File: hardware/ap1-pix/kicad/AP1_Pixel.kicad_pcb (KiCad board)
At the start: 2 copper layers, 88 x 56 mm, 43 parts, among them J1 ENTRADA 5-24V, J2 PIXELES 1, J3 PIXELES 2, J4 PIXELES 3, J5 PIXELES 4, J7 PROGRAMADOR, U1 INA238, U2 LMR16006XDDC, U3 74HCT125D, U4 M24C02-WMN6TP

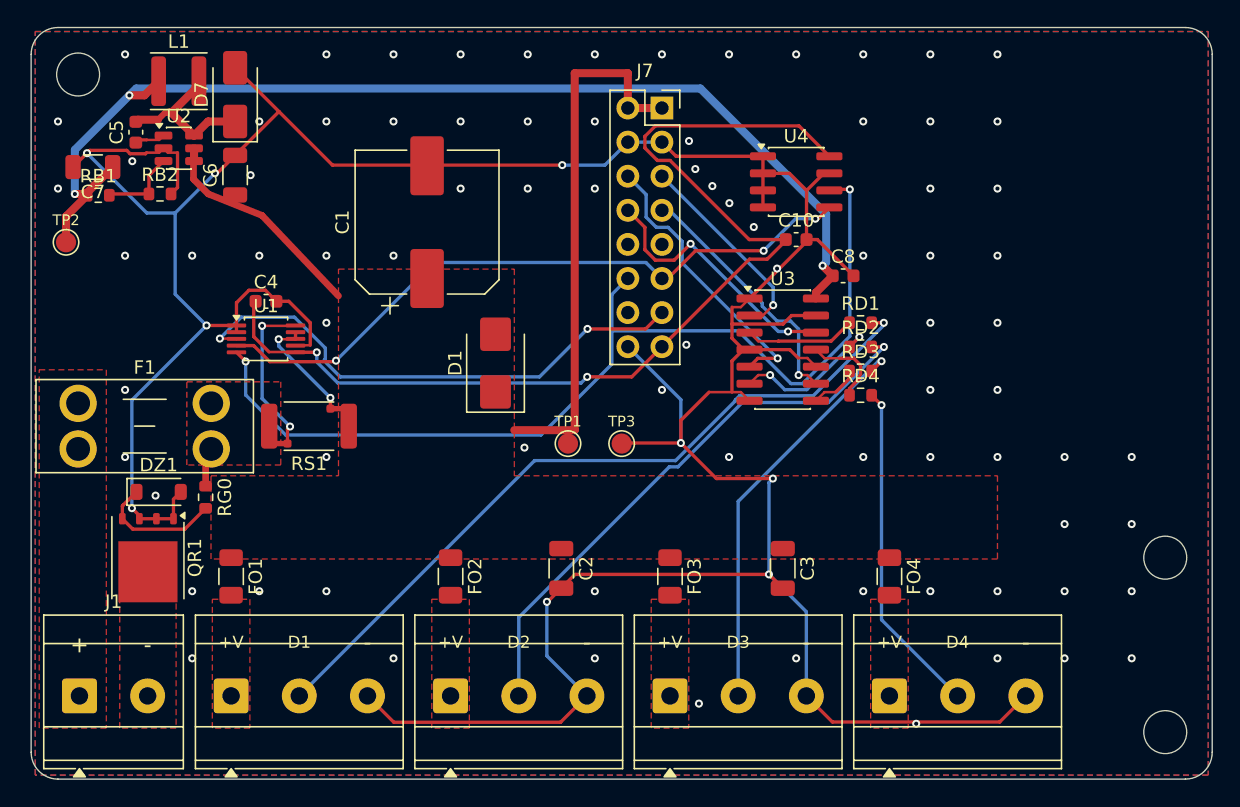
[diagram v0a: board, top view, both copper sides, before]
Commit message: AP CONNECT: sin borneras en todas las placas, placa nueva AP PRO AI4 y guía de fabricantes
- Borneras de tornillo reemplazadas por conectores con cable y código LCSC verificado:
  XT60 (C98732), JST VH 2/3/4 (C160315/6/7), JST XH 2/3/4 (C158012, C144394/5), Qwiic
  en BASE, IND, PIX, DMX, PLANTILLA, AP INPUT, AP OUTPUT y DIST 4; zonas de potencia rehechas
- XT60 de la DIST 4 con la polaridad marcada en la huella (pata 1 = -, pata 2 = +)
- TCA9554PWR ya con código (C477924)
- ap1-ai4: 4 entradas 0-10 V / 4-20 mA con ADS1115 (C37593), +24 V para sensores de lazo
- Programa 1.7: lectura AI4, umbrales con acciones, Home Assistant, tarjeta en la app
- FABRICANTES.md: JLCPCB, PCBWay, Seeed, NextPCB, México; impresión 3D y tornillería
- Pedido JLCPCB con 10 placas (AP-0.2 retirada); ERC/DRC/DFM 0 en todas

Co-Authored-By: Claude Opus 5.5 <noreply@anthropic.com>
Claude-Session: https://claude.ai/code/session_01WVk3oGwfQfGTmAT2PMp8oW
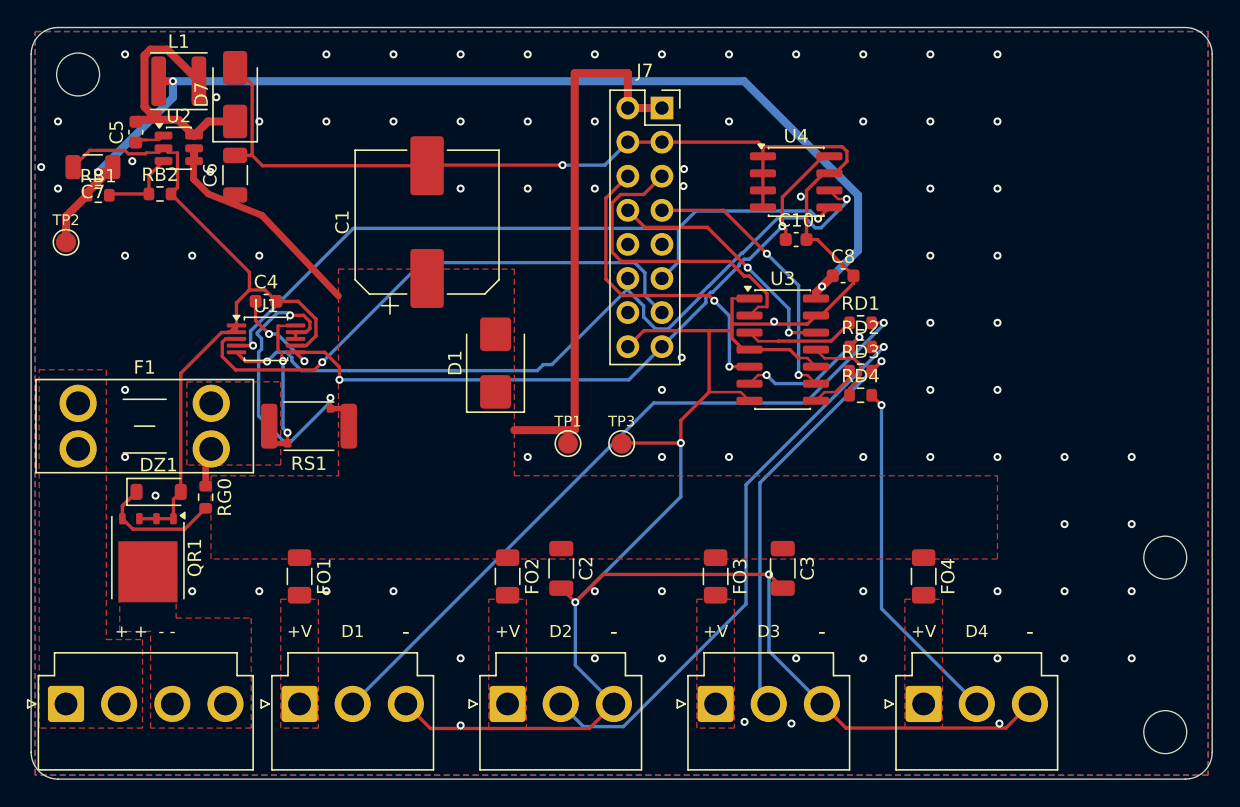
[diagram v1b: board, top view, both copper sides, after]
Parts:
- J1: footprint TerminalBlock_Phoenix:TerminalBlock_Phoenix_MKDS-3-2-5.08_1x02_P5.08mm_Horizontal -> Connector_JST:JST_VH_B4P-VH_1x04_P3.96mm_Vertical
- J2, J3, J4, J5: footprint TerminalBlock_Phoenix:TerminalBlock_Phoenix_MKDS-3-3-5.08_1x03_P5.08mm_Horizontal -> Connector_JST:JST_VH_B3P-VH_1x03_P3.96mm_Vertical
- moved J2 5.14 mm to (120.0, 150.4)
- moved FO1 5.10 mm to (120.0, 140.9)
- moved J3 4.29 mm to (135.5, 150.4)
- moved FO2 4.25 mm to (135.5, 140.9)
- moved J4 3.45 mm to (151.0, 150.4)
- moved FO3 3.40 mm to (151.0, 140.9)
- moved J5 2.62 mm to (166.5, 150.4)
- moved FO4 2.55 mm to (166.5, 140.9)
- moved J1 1.17 mm to (102.6, 150.4)
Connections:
- J1 pad 2: /GNDIN -> /VIN_RAW
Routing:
- net /3V3: track 77.8 -> 58.0 mm, vias 2 -> 4
- net /GND: track 275.7 -> 259.5 mm, vias 91 -> 87
- net /SCL: track 74.4 -> 58.2 mm
- net /ISN: track 8.54 -> 21.9 mm
- net /PWM1: track 15.1 -> 23.6 mm, vias 1 -> 0
- net /SW: track 12.2 -> 19.1 mm
- net /DAT1: track 56.1 -> 52.3 mm
- net /SDA: track 50.4 -> 54.1 mm, vias 3 -> 2
- net /PWM2: track 21.1 -> 24.0 mm, vias 1 -> 2
- net /ALERT: track 39.3 -> 41.3 mm, vias 2 -> 1
- net /ISP: track 12.2 -> 10.4 mm
- net /PWM3: track 19.0 -> 20.7 mm, vias 1 -> 2
- net /DAT4: track 25.1 -> 26.2 mm
- net /PWM4: track 19.8 -> 18.8 mm
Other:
- board text added: "+ + - -"
- board text removed: "+"
